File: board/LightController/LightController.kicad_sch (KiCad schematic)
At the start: 38 parts, among them J1 PJ-051AH, J2 Light bank 1, J3 Light Bank 2, J4 Light Bank 3, U1 CPC1002N, U10 CPC1002N, U11 CPC1002N, U12 FeatherS2, U2 CPC1002N, U3 CPC1002N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

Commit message: Increased caps to 1206.
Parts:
- C1, C3, C4: footprint Capacitor_SMD:C_0805_2012Metric -> Capacitor_SMD:C_1206_3216Metric
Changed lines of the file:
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@@
       (effects (font (size 1.27 1.27)) (justify left))
     )
-    (property "Footprint" "Capacitor_SMD:C_0805_2012Metric" (id 2) (at 113.9952 55.88 0)
+    (property "Footprint" "Capacitor_SMD:C_1206_3216Metric" (id 2) (at 113.9952 55.88 0)
       (effects (font (size 1.27 1.27)) hide)
     )
@@
       (effects (font (size 1.27 1.27)) (justify left))
     )
-    (property "Footprint" "Capacitor_SMD:C_0805_2012Metric" (id 2) (at 124.1552 55.88 0)
+    (property "Footprint" "Capacitor_SMD:C_1206_3216Metric" (id 2) (at 124.1552 55.88 0)
       (effects (font (size 1.27 1.27)) hide)
     )
@@
       (effects (font (size 1.27 1.27)) (justify left))
     )
-    (property "Footprint" "Capacitor_SMD:C_0805_2012Metric" (id 2) (at 49.2252 55.88 0)
+    (property "Footprint" "Capacitor_SMD:C_1206_3216Metric" (id 2) (at 49.2252 55.88 0)
       (effects (font (size 1.27 1.27)) hide)
     )
@@
     )
     (path "/d7d6c6c9-1fda-4dab-8786-779df910db4e"
-      (reference "C1") (unit 1) (value "10µF") (footprint "Capacitor_SMD:C_0805_2012Metric")
+      (reference "C1") (unit 1) (value "10µF") (footprint "Capacitor_SMD:C_1206_3216Metric")
     )
     (path "/cda0317e-3a0c-49d7-a2c3-a3d5423dfa4d"
@@
     )
     (path "/358be4dc-9ae7-42fb-bb5f-97253842315f"
-      (reference "C3") (unit 1) (value "22µF") (footprint "Capacitor_SMD:C_0805_2012Metric")
+      (reference "C3") (unit 1) (value "22µF") (footprint "Capacitor_SMD:C_1206_3216Metric")
     )
     (path "/8da86106-0751-4439-acdd-3f37b2dbfba6"
-      (reference "C4") (unit 1) (value "22µF") (footprint "Capacitor_SMD:C_0805_2012Metric")
+      (reference "C4") (unit 1) (value "22µF") (footprint "Capacitor_SMD:C_1206_3216Metric")
     )
     (path "/5fdabda6-9c9c-427b-87e5-a291030a9854"

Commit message: Increased inductor size to 1206.
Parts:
- L1: footprint Inductor_SMD:L_0805_2012Metric -> Inductor_SMD:L_1206_3216Metric
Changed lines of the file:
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@@
     (property "Reference" "L1" (id 0) (at 102.87 38.1 90))
     (property "Value" "8.7µH" (id 1) (at 102.87 40.64 90))
-    (property "Footprint" "Inductor_SMD:L_0805_2012Metric" (id 2) (at 102.87 44.45 0)
+    (property "Footprint" "Inductor_SMD:L_1206_3216Metric" (id 2) (at 102.87 44.45 0)
       (effects (font (size 1.27 1.27)) hide)
     )
@@
     )
     (path "/4af9f695-9d31-47b7-9c1e-fff616a0e148"
-      (reference "L1") (unit 1) (value "8.7µH") (footprint "Inductor_SMD:L_0805_2012Metric")
+      (reference "L1") (unit 1) (value "8.7µH") (footprint "Inductor_SMD:L_1206_3216Metric")
     )
     (path "/d450be2c-5607-4e49-82b4-991878978321"

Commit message: Changed Inductor value to 8.2µH.
Matches the component ordered as 8.7µH is an uncommon value.
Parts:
- L1: value 8.7µH -> 8.2µH
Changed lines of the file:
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@@
     (in_bom yes) (on_board yes) (fields_autoplaced)
     (property "Reference" "L1" (id 0) (at 102.87 38.1 90))
-    (property "Value" "8.7µH" (id 1) (at 102.87 40.64 90))
+    (property "Value" "8.2µH" (id 1) (at 102.87 40.64 90))
     (property "Footprint" "Inductor_SMD:L_1206_3216Metric" (id 2) (at 102.87 44.45 0)
       (effects (font (size 1.27 1.27)) hide)
@@
     )
     (path "/4af9f695-9d31-47b7-9c1e-fff616a0e148"
-      (reference "L1") (unit 1) (value "8.7µH") (footprint "Inductor_SMD:L_1206_3216Metric")
+      (reference "L1") (unit 1) (value "8.2µH") (footprint "Inductor_SMD:L_1206_3216Metric")
     )
     (path "/d450be2c-5607-4e49-82b4-991878978321"

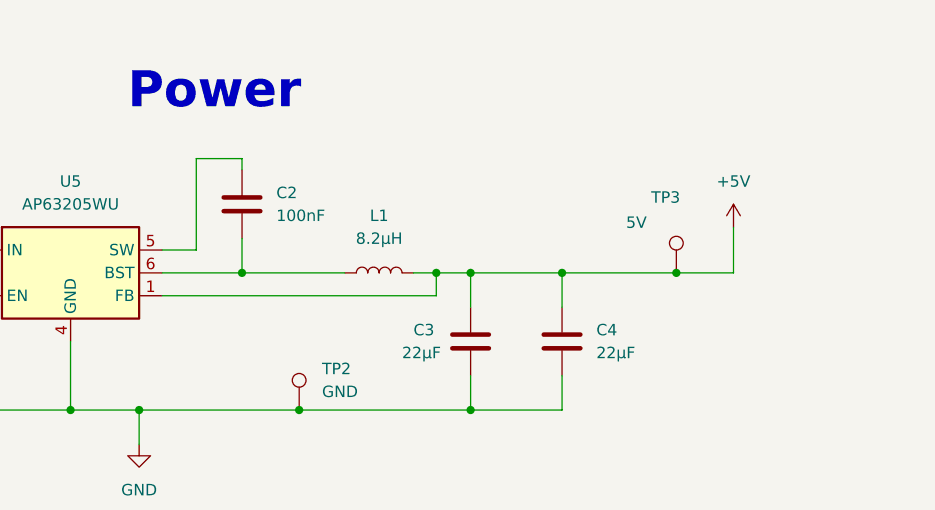
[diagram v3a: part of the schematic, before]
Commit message: Fixed pin 5/6 swap design issue.
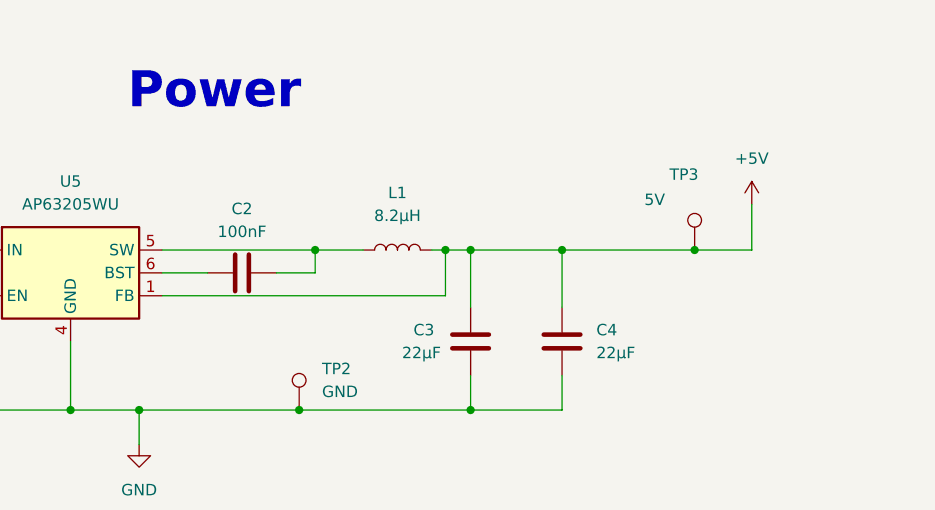
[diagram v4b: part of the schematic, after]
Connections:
- net at C2.2, L1.1: now also U5.5 (SW); no longer U5.6 (BST)
- net at C2.1: now also U5.6 (BST); no longer U5.5 (SW)
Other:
- moved on the sheet: C2, L1, TP3
